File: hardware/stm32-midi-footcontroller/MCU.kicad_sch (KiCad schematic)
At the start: 0 parts

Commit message: begin work on MCU schematic page
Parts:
- added C? (x2): 1u, symbol Device:C
- added C? (x5): 100n, symbol Device:C
- added C?: 10u, symbol Device:C
- added C? (x2): 10p, symbol Device:C
- added C?: 10n, symbol Device:C
- added C?: C, symbol Device:C
- added FB?: 120R, symbol Device:FerriteBead
- added J?: TC2030, Connector:Tag-Connect_TC2030-IDC-FP_2x03_P1.27mm_Vertical, symbol midi-library:TC2030
- added J?: USB_OTG, symbol Connector:USB_OTG
- added R?: 100k, symbol Device:R
- added U?: STM32F412RETx, Package_QFP:LQFP-64_10x10mm_P0.5mm, symbol MCU_ST_STM32F4:STM32F412RETx
- added Y?: 16MHz, symbol Device:Crystal_GND24
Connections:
- new net +3.3VA: C?.1, C?.1, FB?.1, U?.13 (VDDA)
- new net +3V3: C?.1, C?.1, C?.1, C?.1, C?.1, C?.1, C?.1, FB?.2, J?.1 (VCC), R?.1, U?.1 (VBAT), U?.19 (VDD), U?.32 (VDD), U?.48 (VDD), U?.64 (VDD)
- new net GND: C?.2, C?.2, C?.2, C?.2, C?.2, C?.2, C?.2, C?.2, C?.2, C?.2, C?.2, C?.2, J?.5 (GND), U?.12 (VSSA), U?.18 (VSS), U?.31 (VSS), U?.47 (VSS), U?.63 (VSS), Y?.2, Y?.4
- new net HSE_IN: C?.1, U?.5 (PH0), Y?.1
- new net HSE_OUT: C?.1, U?.6 (PH1), Y?.3
- new net SWCLK: J?.4 (SWCLK/TCK), U?.49 (PA14)
- new net SWDIO: J?.2 (SWDIO/TMS), U?.46 (PA13)
- new net SWO: J?.6 (SWO/TDO), U?.55 (PB3)
- new net USB_D+: J?.3 (D+), U?.45 (PA12)
- new net USB_D-: J?.2 (D-), U?.44 (PA11)
- new net USB_ID: J?.4 (ID), U?.43 (PA10)
- new net nRESET: C?.1, J?.3 (nRESET), R?.2, U?.7 (NRST)
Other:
- note added: "Need to investigate voltage sourcing involved with USB Host for MIDI"

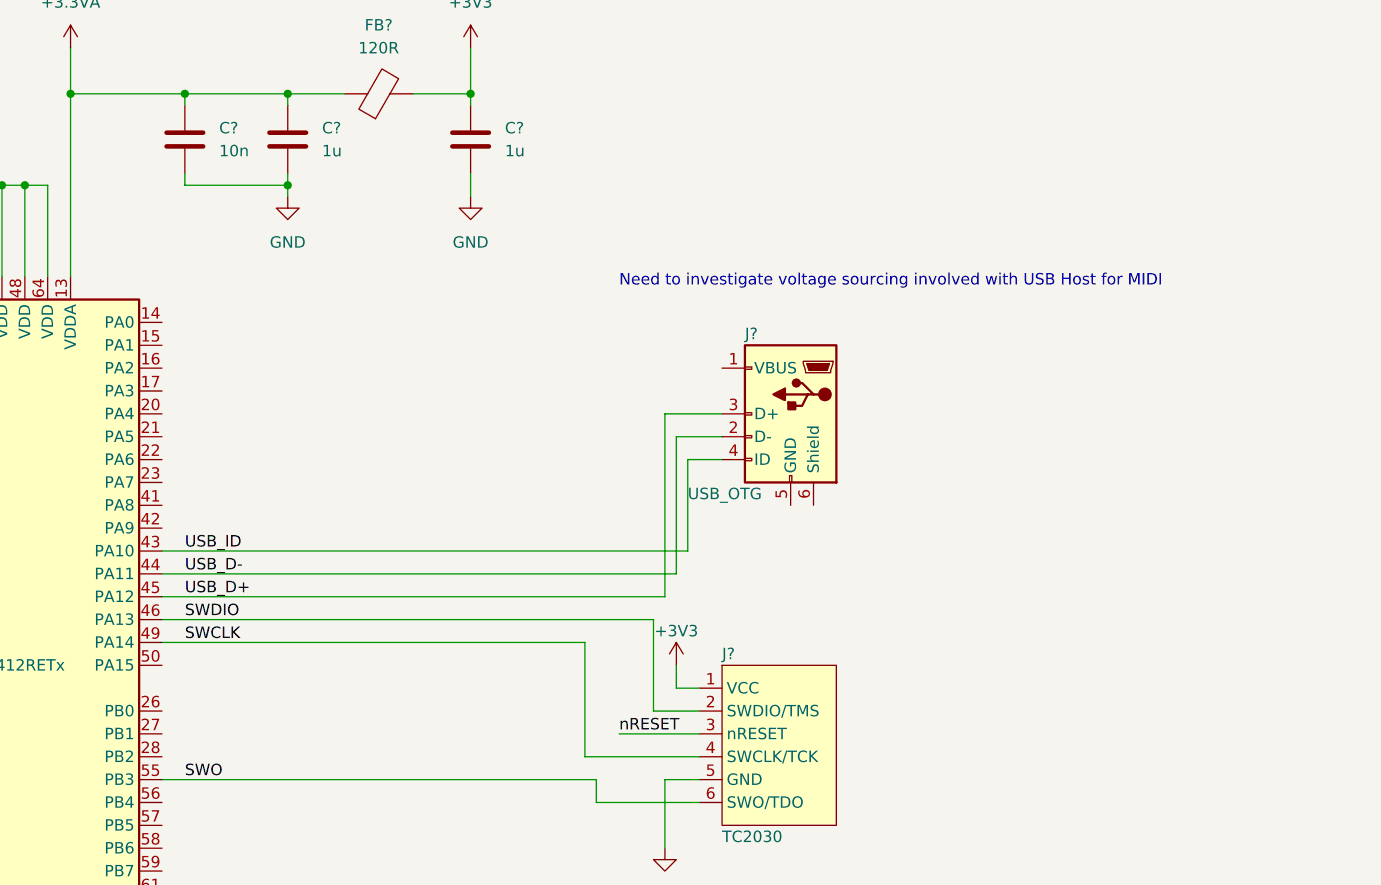
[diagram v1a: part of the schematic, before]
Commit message: add 5v rail, fill out usb host, add usb vout smart fet to library
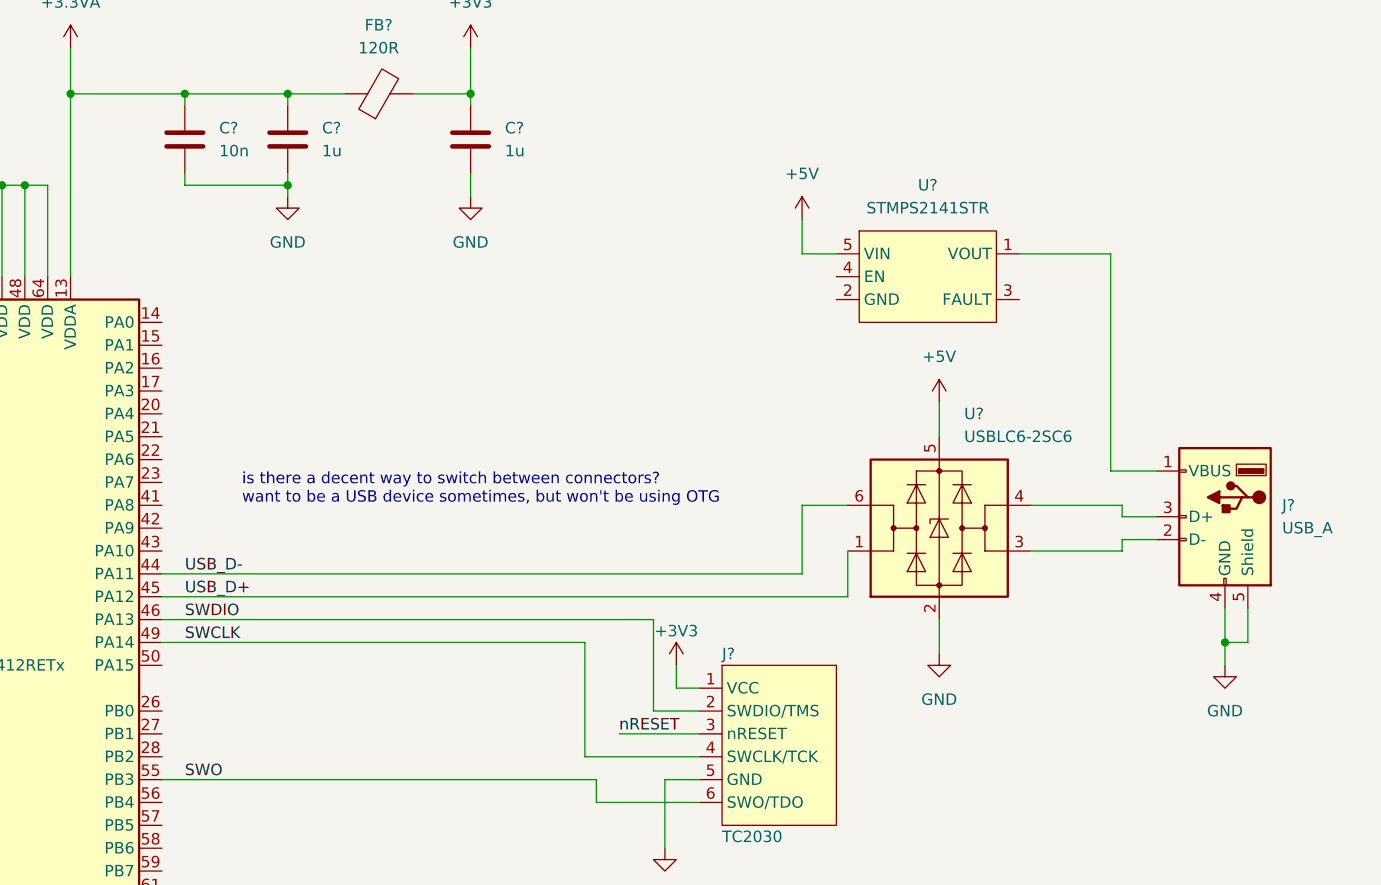
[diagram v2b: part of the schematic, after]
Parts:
- removed J?: USB_OTG, symbol Connector:USB_OTG
- added J?: USB_A, symbol Connector:USB_A
- added U?: USBLC6-2SC6, Package_TO_SOT_SMD:SOT-23-6, symbol Power_Protection:USBLC6-2SC6
- added U?: STMPS2141STR, symbol midi-library:STMPS2141STR
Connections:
- net GND: now also J?.4 (GND), J?.5 (Shield), U?.2 (GND)
- net USB_D+: now also U?.1 (I/O1)
- net USB_D-: now also U?.6 (I/O1)
- net USB_ID: no longer names the net of U?.43 (PA10)
- new net: J?.2 (D-), U?.3 (I/O2)
- new net: J?.3 (D+), U?.4 (I/O2)
- new net: J?.1 (VBUS), U?.1 (VOUT)
- new net +5V: U?.5 (VBUS), U?.5 (VIN)
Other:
- note added: "is there a decent way to switch between connectors? want to be a USB device sometimes, but won't be using OTG"
- note removed: "Need to investigate voltage sourcing involved with USB Host for MIDI"

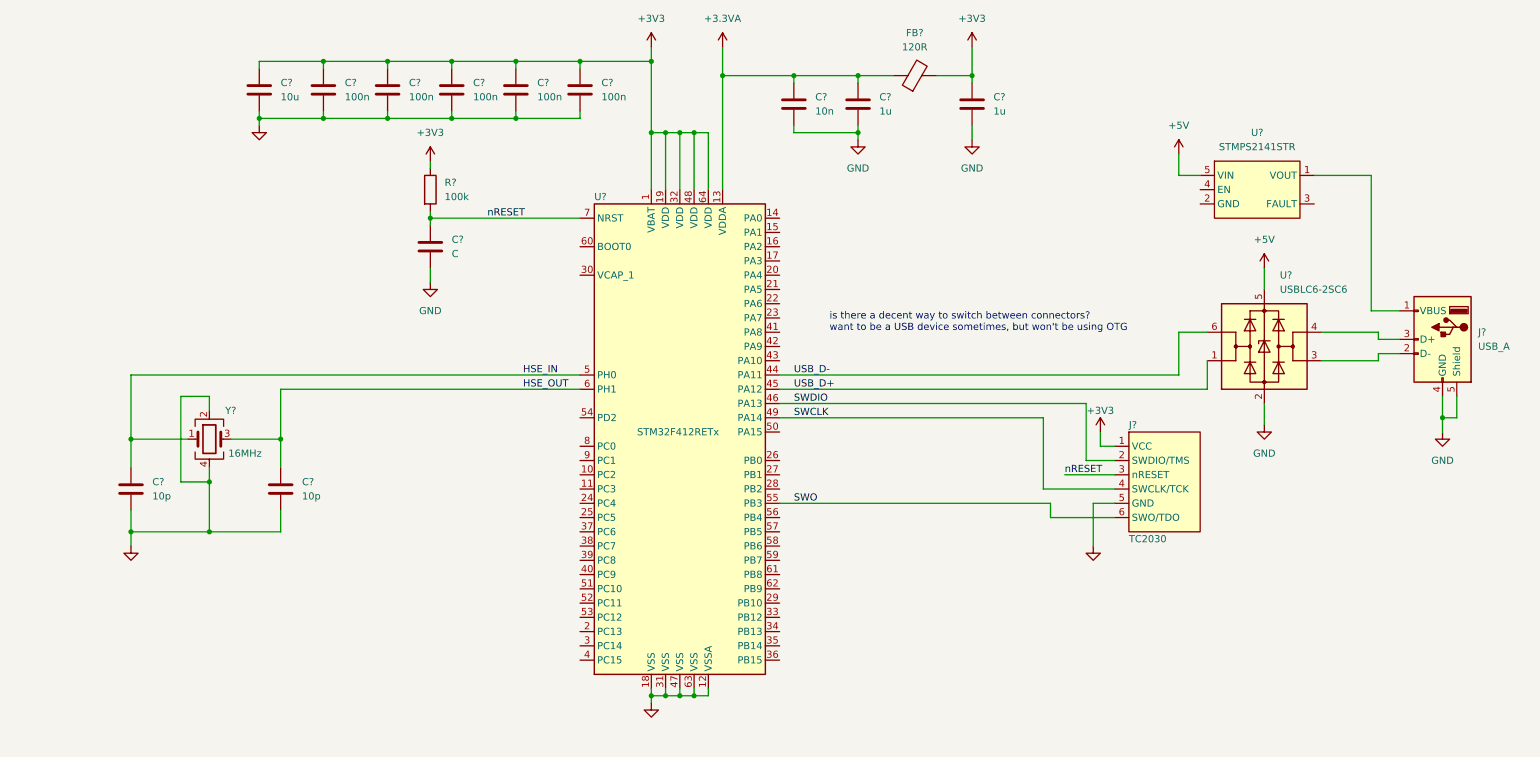
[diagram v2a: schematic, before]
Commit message: add USB host and device connectors to schematic
added low Ron spdt multiplexer to symbol library, connected USB D+/D- through a pair of them to device and host connectrors. Added USB Host 5v out enable GPIO
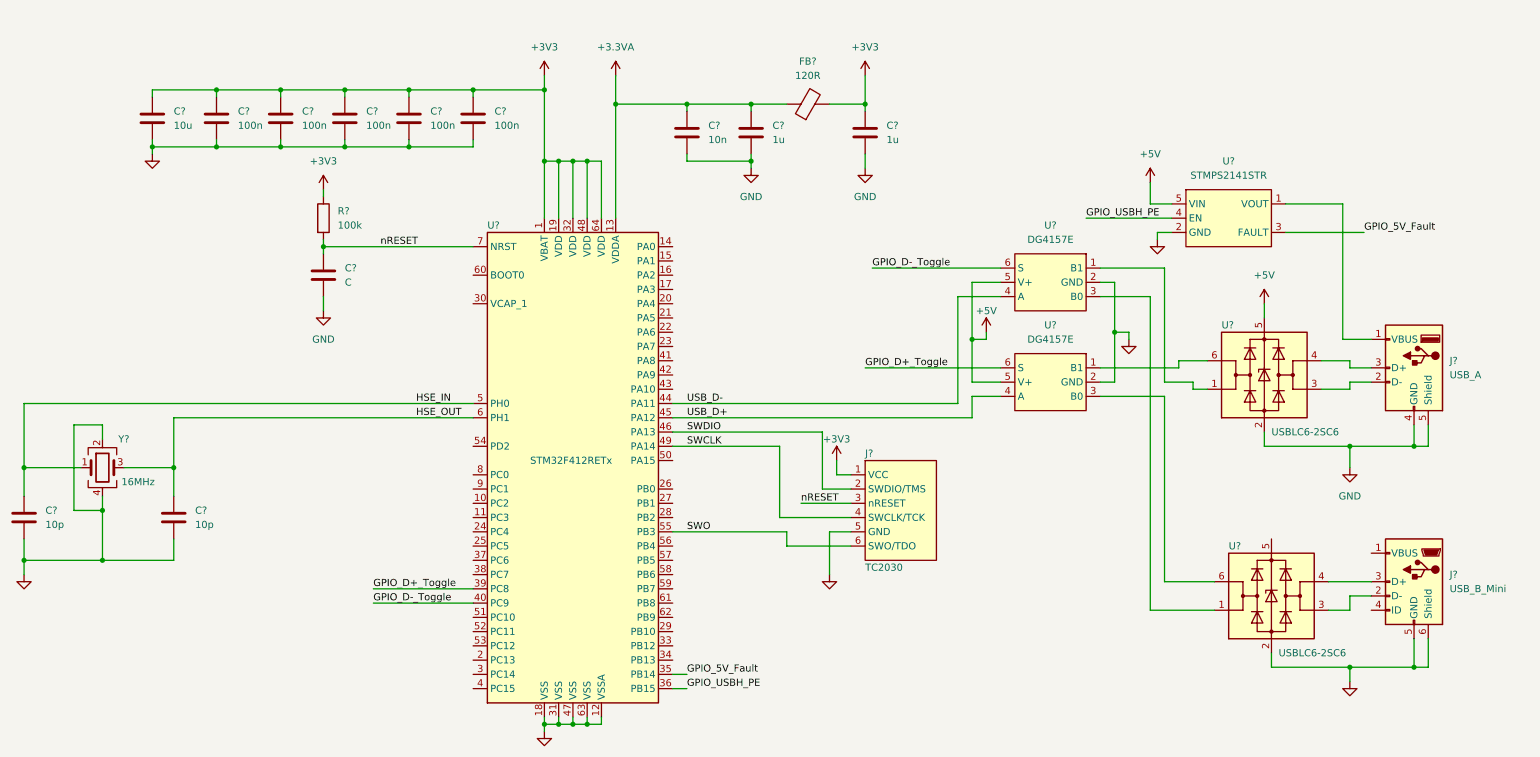
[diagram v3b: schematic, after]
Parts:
- added J?: USB_B_Mini, symbol Connector:USB_B_Mini
- added U? (x2): DG4157E, symbol midi-library:DG4157E
- added U?: USBLC6-2SC6, Package_TO_SOT_SMD:SOT-23-6, symbol Power_Protection:USBLC6-2SC6
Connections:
- net +5V: now also U?.5 (V+), U?.5 (V+)
- net GND: now also U?.2 (GND), J?.5 (GND), J?.6 (Shield), U?.2 (GND), U?.2 (GND), U?.2 (GND)
- net USB_D+: now also U?.4 (A); no longer U?.1 (I/O1)
- net USB_D-: now also U?.4 (A); no longer U?.6 (I/O1)
- net GPIO_5V_Fault: now reaches U?.35 (PB14)
- net GPIO_5V_Fault: now also U?.3 (FAULT)
- net GPIO_USBH_PE: now reaches U?.36 (PB15)
- net GPIO_USBH_PE: now also U?.4 (EN)
- net GPIO_D+_Toggle: now reaches U?.39 (PC8)
- net GPIO_D+_Toggle: now also U?.6 (S)
- net GPIO_D-_Toggle: now reaches U?.40 (PC9)
- net GPIO_D-_Toggle: now also U?.6 (S)
- new net: U?.1 (B1), U?.1 (I/O1)
- new net: U?.1 (I/O1), U?.3 (B0)
- new net: U?.1 (B1), U?.6 (I/O1)
- new net: U?.3 (B0), U?.6 (I/O1)
- new net: J?.2 (D-), U?.3 (I/O2)
- new net: J?.3 (D+), U?.4 (I/O2)
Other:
- note removed: "is there a decent way to switch between connectors? want to be a USB device sometimes, but won't be using OTG"
- moved on the sheet: C?, FB?, J?, R?, U?, Y?

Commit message: add midi hardware to schematic
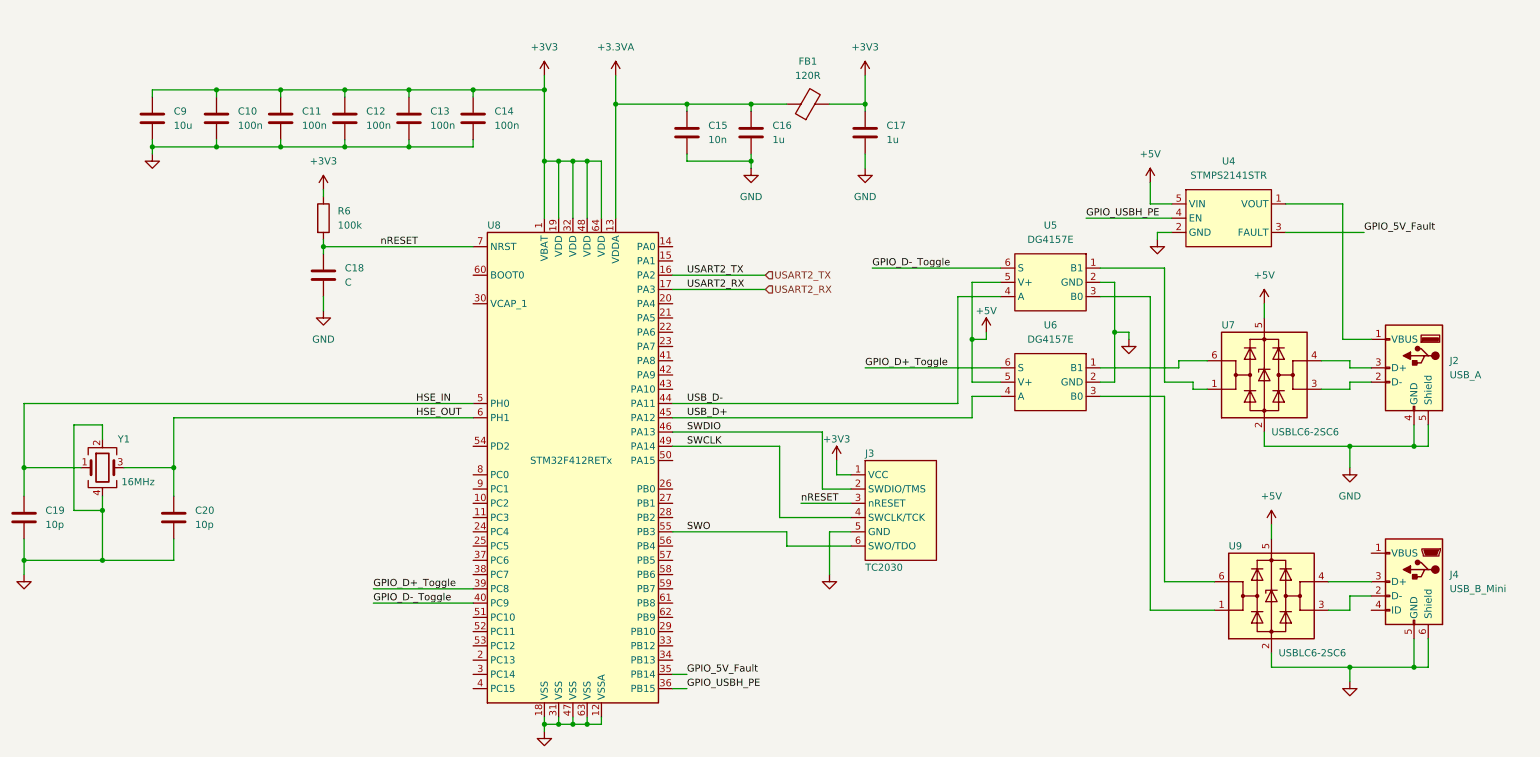
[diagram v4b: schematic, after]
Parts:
- gave numbers to parts that had none: 24
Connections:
- net +5V: now also U9.5 (VBUS)
- net USART2_TX: now reaches U8.16 (PA2)
- net USART2_RX: now reaches U8.17 (PA3)
